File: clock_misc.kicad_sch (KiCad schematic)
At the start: 12 parts, among them Y1 Osc60MHz

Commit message: schematic wip
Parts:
- removed C56: 0.1uF, Capacitor_SMD:C_0402_1005Metric, symbol Device:C
- removed FID1, FID2, FID3, FID4: Fiducial, Fiducial:Fiducial_0.5mm_Mask1mm, symbol Mechanical:Fiducial
- removed Y1: Osc60MHz, Crystal:Crystal_SMD_3225-4Pin_3.2x2.5mm, symbol support_hardware:DSC60xx
- added C159 (x3), C39 (x2): 1uF, Capacitor_SMD:C_0402_1005Metric, symbol Device:C
- added R103, R104, R105, R106, R34, R35, R36: 330, Resistor_SMD:R_0402_1005Metric, symbol Device:R
- added U19 (x2): 74LVC1G06, Package_TO_SOT_SMD:SOT-353_SC-70-5, symbol 74xGxx:74LVC1G06
- added U20: 74LVC1G80, Package_TO_SOT_SMD:SOT-353_SC-70-5, symbol 74xGxx:74AUP1G80
- added U21: FANOUT, symbol support_hardware:74AVC9112
- added Y1: TCXO, Oscillator:Oscillator_SMD_Kyocera_KC2520Z-4Pin_2.5x2.0mm, symbol Oscillator:SG-210SCD
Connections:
- net +3V3: now also C39.1, C39.1, U21.1 (VCC), Y1.1 (OE), Y1.4 (Vcc)
- net GND: now also C159.2, C159.2, C159.2, C39.2, C39.2, U19.3 (GND), U19.3 (GND), U20.3 (GND), U21.3 (~{OE}), U21.4 (GND), Y1.2 (GND)
- net FPGA_CLK: now reaches R45.2
- net CLOCK_60MHZ: no longer names the net of TP34.1
- net CLOCK_60MHZ: now also U21.2 (A), Y1.3 (OUT); no longer R45.1
- new net: R105.1, U21.5 (Y1)
- new net: R104.1, U21.6 (Y2)
- new net: R103.1, U21.7 (Y3)
- new net: R45.1, U21.8 (Y4)
- new net: R36.2, U20.1 (D), U20.4 (~{Q})
- new net: R34.1, R35.1, U19.4
- new net: R106.1, U19.4
- new net 3V3RX: C159.1, C159.1, U19.5 (VCC), U20.5 (VCC)
- new net 3V3TX: C159.1, U19.5 (VCC)
- new net AFE_CLK: R103.2
- new net RX_CLK: R104.2, U19.2, U20.2 (C)
- new net RX_MIX_CLK: R106.2
- new net RX_RCVR_CLK: R36.1
- new net TX_CLK: R105.2, U19.2
- new net TX_MIX_CLK: R35.2
- new net TX_XCVR_CLK: R34.2
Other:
- moved on the sheet: H1, H2, H3, H4, R45, TP34

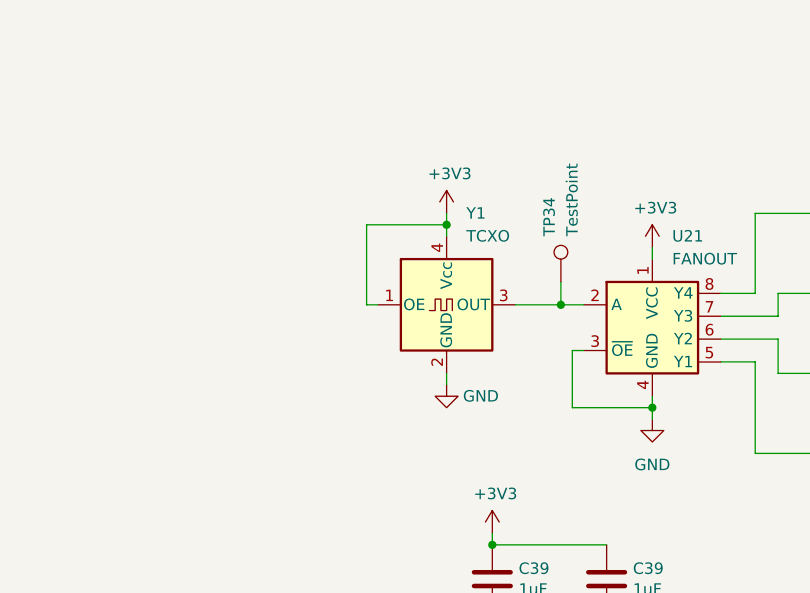
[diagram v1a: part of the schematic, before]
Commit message: add SWH two-way RF test connectors
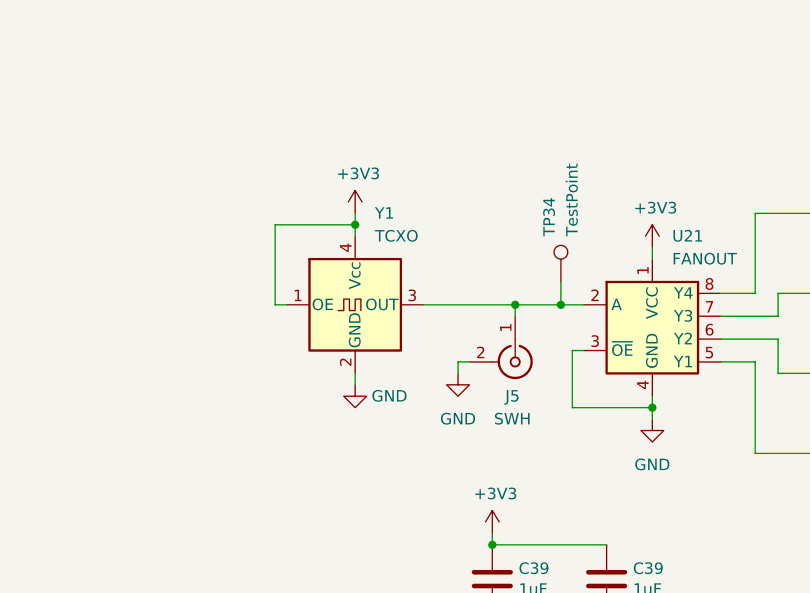
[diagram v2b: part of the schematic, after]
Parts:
- added J5: SWH, symbol Connector:Conn_Coaxial
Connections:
- net GND: now also J5.2 (Ext)
- net at TP34.1, U21.2 (A), Y1.3 (OUT): now also J5.1 (In)
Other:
- moved on the sheet: Y1
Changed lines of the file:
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@@
   (junction (at 241.3 77.47) (diameter 0) (color 0 0 0 0)
   )
-  (junction (at 71.12 67.31) (diameter 0) (color 0 0 0 0)
+  (junction (at 60.96 67.31) (diameter 0) (color 0 0 0 0)
   )
   (junction (at 173.99 123.19) (diameter 0) (color 0 0 0 0)
   )
+  (junction (at 78.74 76.2) (diameter 0) (color 0 0 0 0)
+  )
   (junction (at 40.64 168.91) (diameter 0) (color 0 0 0 0)
   )
@@
     (stroke (width 0) (type default))
   )
-  (wire (pts (xy 63.5 76.2) (xy 62.23 76.2))
+  (wire (pts (xy 53.34 76.2) (xy 52.07 76.2))
+    (stroke (width 0) (type default))
+  )
+  (wire (pts (xy 72.39 82.55) (xy 72.39 83.82))
     (stroke (width 0) (type default))
   )
@@
     (stroke (width 0) (type default))
   )
-  (wire (pts (xy 71.12 67.31) (xy 71.12 68.58))
+  (wire (pts (xy 78.74 76.2) (xy 83.82 76.2))
+    (stroke (width 0) (type default))
+  )
+  (wire (pts (xy 60.96 67.31) (xy 60.96 68.58))
     (stroke (width 0) (type default))
   )
@@
     (stroke (width 0) (type default))
   )
-  (wire (pts (xy 71.12 66.04) (xy 71.12 67.31))
+  (wire (pts (xy 60.96 66.04) (xy 60.96 67.31))
     (stroke (width 0) (type default))
   )
@@
     (stroke (width 0) (type default))
   )
-  (wire (pts (xy 62.23 76.2) (xy 62.23 67.31))
+  (wire (pts (xy 52.07 76.2) (xy 52.07 67.31))
     (stroke (width 0) (type default))
   )
@@
     (stroke (width 0) (type default))
   )
+  (wire (pts (xy 73.66 82.55) (xy 72.39 82.55))
+    (stroke (width 0) (type default))
+  )
   (wire (pts (xy 143.51 39.37) (xy 143.51 22.86))
     (stroke (width 0) (type default))
@@
     (stroke (width 0) (type default))
   )
-  (wire (pts (xy 78.74 76.2) (xy 83.82 76.2))
+  (wire (pts (xy 68.58 76.2) (xy 78.74 76.2))
     (stroke (width 0) (type default))
   )
@@
     (stroke (width 0) (type default))
   )
+  (wire (pts (xy 78.74 76.2) (xy 78.74 77.47))
+    (stroke (width 0) (type default))
+  )
   (wire (pts (xy 119.38 83.82) (xy 143.51 83.82))
     (stroke (width 0) (type default))
@@
     (stroke (width 0) (type default))
   )
-  (wire (pts (xy 62.23 67.31) (xy 71.12 67.31))
+  (wire (pts (xy 52.07 67.31) (xy 60.96 67.31))
     (stroke (width 0) (type default))
   )
@@
     (stroke (width 0) (type default))
   )
-  (wire (pts (xy 71.12 85.09) (xy 71.12 83.82))
+  (wire (pts (xy 60.96 85.09) (xy 60.96 83.82))
     (stroke (width 0) (type default))
   )
@@
     )
   )
-  (symbol (lib_id "power:+3V3") (at 71.12 66.04 0) (unit 1)
+  (symbol (lib_id "power:+3V3") (at 60.96 66.04 0) (unit 1)
     (in_bom yes) (on_board yes) (dnp no)
-    (property "Reference" "#PWR0170" (at 71.12 69.85 0)
-      (effects (font (size 1.27 1.27)) hide)
-    )
-    (property "Value" "+3V3" (at 71.4756 61.6458 0)
-      (effects (font (size 1.27 1.27)))
-    )
-    (property "Footprint" "" (at 71.12 66.04 0)
-      (effects (font (size 1.27 1.27)) hide)
-    )
-    (property "Datasheet" "" (at 71.12 66.04 0)
+    (property "Reference" "#PWR0170" (at 60.96 69.85 0)
+      (effects (font (size 1.27 1.27)) hide)
+    )
+    (property "Value" "+3V3" (at 61.3156 61.6458 0)
+      (effects (font (size 1.27 1.27)))
+    )
+    (property "Footprint" "" (at 60.96 66.04 0)
+      (effects (font (size 1.27 1.27)) hide)
+    )
+    (property "Datasheet" "" (at 60.96 66.04 0)
       (effects (font (size 1.27 1.27)) hide)
     )
@@
     )
   )
+  (symbol (lib_id "Connector:Conn_Coaxial") (at 78.74 82.55 270) (unit 1)
+    (in_bom yes) (on_board yes) (dnp no) (fields_autoplaced)
+    (property "Reference" "J5" (at 78.4468 86.36 90)
+      (effects (font (size 1.27 1.27)))
+    )
+    (property "Value" "SWH" (at 78.4468 88.9 90)
+      (effects (font (size 1.27 1.27)))
+    )
+    (property "Footprint" "" (at 78.74 82.55 0)
+      (effects (font (size 1.27 1.27)) hide)
+    )
+    (property "Datasheet" " ~" (at 78.74 82.55 0)
+      (effects (font (size 1.27 1.27)) hide)
+    )
+    (property "Description" "COAX CONN TWO-WAY" (at 78.74 82.55 0)
+      (effects (font (size 1.27 1.27)) hide)
+    )
+    (property "Manufacturer" "Murata" (at 78.74 82.55 0)
+      (effects (font (size 1.27 1.27)) hide)
+    )
+    (property "Part Number" "MM8930-2620RJ4" (at 78.74 82.55 0)
+      (effects (font (size 1.27 1.27)) hide)
+    )
+    (property "Substitution" "MM8930-2620RK15" (at 78.74 82.55 0)
+      (effects (font (size 1.27 1.27)) hide)
+    )
+    (pin "1")
+    (pin "2")
+    (instances
+      (project "mainboard"
+        (path "/fb621148-8145-4217-9712-738e1b5a4823/4ec621be-184d-4855-a96d-f6fa2a788a77/90da2209-0e18-4bd4-8ef6-3d6f9ed46ff8"
+          (reference "J5") (unit 1)
+        )
+        (path "/fb621148-8145-4217-9712-738e1b5a4823/4ec621be-184d-4855-a96d-f6fa2a788a77/6aa278c8-8281-4438-81b7-90e6d7ac4f12"
+          (reference "J11") (unit 1)
+        )
+        (path "/fb621148-8145-4217-9712-738e1b5a4823/07741d92-cb3b-401f-9c7e-29f688af7269"
+          (reference "J12") (unit 1)
+        )
+      )
+    )
+  )
   (symbol (lib_id "support_hardware:3V3TX") (at 154.94 111.76 0) (unit 1)
     (in_bom yes) (on_board yes) (dnp no) (fields_autoplaced)
@@
     )
   )
-  (symbol (lib_id "power:GND") (at 71.12 85.09 0) (unit 1)
+  (symbol (lib_id "power:GND") (at 60.96 85.09 0) (unit 1)
     (in_bom yes) (on_board yes) (dnp no)
-    (property "Reference" "#PWR0173" (at 71.12 91.44 0)
-      (effects (font (size 1.27 1.27)) hide)
-    )
-    (property "Value" "GND" (at 74.93 86.36 0)
-      (effects (font (size 1.27 1.27)))
-    )
-    (property "Footprint" "" (at 71.12 85.09 0)
-      (effects (font (size 1.27 1.27)) hide)
-    )
-    (property "Datasheet" "" (at 71.12 85.09 0)
+    (property "Reference" "#PWR0173" (at 60.96 91.44 0)
+      (effects (font (size 1.27 1.27)) hide)
+    )
+    (property "Value" "GND" (at 64.77 86.36 0)
+      (effects (font (size 1.27 1.27)))
+    )
+    (property "Footprint" "" (at 60.96 85.09 0)
+      (effects (font (size 1.27 1.27)) hide)
+    )
+    (property "Datasheet" "" (at 60.96 85.09 0)
       (effects (font (size 1.27 1.27)) hide)
     )
@@
     )
   )
-  (symbol (lib_id "Oscillator:SG-210SCD") (at 71.12 76.2 0) (unit 1)
-    (in_bom yes) (on_board yes) (dnp no) (fields_autoplaced)
-    (property "Reference" "Y1" (at 73.3141 66.04 0)
-      (effects (font (size 1.27 1.27)) (justify left))
-    )
-    (property "Value" "TCXO" (at 73.3141 68.58 0)
-      (effects (font (size 1.27 1.27)) (justify left))
-    )
-    (property "Footprint" "Oscillator:Oscillator_SMD_Kyocera_KC2520Z-4Pin_2.5x2.0mm" (at 71.12 95.25 0)
-      (effects (font (size 1.27 1.27)) hide)
-    )
-    (property "Datasheet" "https://www.raltron.com/webproducts/specs/TCXO/RTXE-2520ED333-C-40.000-TR.pdf" (at 71.12 76.2 0)
-      (effects (font (size 1.27 1.27)) hide)
-    )
-    (property "Description" "XTAL OSC TCXO 40MHZ 3.3V HCMOS" (at 71.12 76.2 0)
-      (effects (font (size 1.27 1.27)) hide)
-    )
-    (property "Manufacturer" "Raltron" (at 71.12 76.2 0)
-      (effects (font (size 1.27 1.27)) hide)
-    )
-    (property "Part Number" "RTXE-2520ED333-C-40.000-TR" (at 71.12 76.2 0)
-      (effects (font (size 1.27 1.27)) hide)
-    )
+  (symbol (lib_id "power:GND") (at 72.39 83.82 0) (unit 1)
+    (in_bom yes) (on_board yes) (dnp no) (fields_autoplaced)
+    (property "Reference" "#PWR023" (at 72.39 90.17 0)
+      (effects (font (size 1.27 1.27)) hide)
+    )
+    (property "Value" "GND" (at 72.39 88.9 0)
+      (effects (font (size 1.27 1.27)))
+    )
+    (property "Footprint" "" (at 72.39 83.82 0)
+      (effects (font (size 1.27 1.27)) hide)
+    )
+    (property "Datasheet" "" (at 72.39 83.82 0)
+      (effects (font (size 1.27 1.27)) hide)
+    )
+    (pin "1")
+    (instances
+      (project "ununs"
+        (path "/a05d7640-f2f6-4ba7-8c51-5a4af431fc13"
+          (reference "#PWR023") (unit 1)
+        )
+      )
+      (project "mainboard"
+        (path "/fb621148-8145-4217-9712-738e1b5a4823/4ec621be-184d-4855-a96d-f6fa2a788a77/90da2209-0e18-4bd4-8ef6-3d6f9ed46ff8"
+          (reference "#PWR0158") (unit 1)
+        )
+        (path "/fb621148-8145-4217-9712-738e1b5a4823/4ec621be-184d-4855-a96d-f6fa2a788a77/6aa278c8-8281-4438-81b7-90e6d7ac4f12"
+          (reference "#PWR0303") (unit 1)
+        )
+        (path "/fb621148-8145-4217-9712-738e1b5a4823/07741d92-cb3b-401f-9c7e-29f688af7269"
+          (reference "#PWR0304") (unit 1)
+        )
+      )
+    )
+  )
+  (symbol (lib_id "Oscillator:SG-210SCD") (at 60.96 76.2 0) (unit 1)
+    (in_bom yes) (on_board yes) (dnp no) (fields_autoplaced)
+    (property "Reference" "Y1" (at 63.1541 66.04 0)
+      (effects (font (size 1.27 1.27)) (justify left))
+    )
+    (property "Value" "TCXO" (at 63.1541 68.58 0)
+      (effects (font (size 1.27 1.27)) (justify left))
+    )
+    (property "Footprint" "Oscillator:Oscillator_SMD_Kyocera_KC2520Z-4Pin_2.5x2.0mm" (at 60.96 95.25 0)
+      (effects (font (size 1.27 1.27)) hide)
+    )
+    (property "Datasheet" "https://www.raltron.com/webproducts/specs/TCXO/RTXE-2520ED333-C-40.000-TR.pdf" (at 60.96 76.2 0)
+      (effects (font (size 1.27 1.27)) hide)
+    )
+    (property "Description" "XTAL OSC TCXO 40MHZ 3.3V HCMOS" (at 60.96 76.2 0)
+      (effects (font (size 1.27 1.27)) hide)
+    )
+    (property "Manufacturer" "Raltron" (at 60.96 76.2 0)
+      (effects (font (size 1.27 1.27)) hide)
+    )
+    (property "Part Number" "RTXE-2520ED333-C-40.000-TR" (at 60.96 76.2 0)
+      (effects (font (size 1.27 1.27)) hide)
+    )

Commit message: update symbol metadata
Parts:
- U21: Manufacturer (none) -> Nexperia; Part Number (none) -> 74AVC9112GTX
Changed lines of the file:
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@@
       (effects (font (size 1.27 1.27)) hide)
     )
-    (property "Datasheet" "" (at 93.98 78.74 0)
+    (property "Datasheet" "https://assets.nexperia.com/documents/data-sheet/74AVC9112.pdf" (at 93.98 78.74 0)
       (effects (font (size 1.27 1.27)) hide)
     )
+    (property "Manufacturer" "Nexperia" (at 93.98 78.74 0)
+      (effects (font (size 1.27 1.27)) hide)
+    )
+    (property "Description" "IC CLK BUFFER 1:4 8XSON" (at 93.98 78.74 0)
+      (effects (font (size 1.27 1.27)) hide)
+    )
+    (property "Part Number" "74AVC9112GTX" (at 93.98 78.74 0)
+      (effects (font (size 1.27 1.27)) hide)
+    )

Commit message: add SWH connector symbols
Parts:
- removed J5: SWH, symbol Connector:Conn_Coaxial
- added J5: SWH, symbol radio:Conn_Coaxial_MM8930-2620
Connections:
- net GND: now also J5.3 (Ext)
- net at TP34.1, U21.2 (A): now also J5.2 (R); no longer Y1.3 (OUT)
- new net: J5.1 (C), Y1.3 (OUT)
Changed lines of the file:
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@@
   (junction (at 173.99 123.19) (diameter 0) (color 0 0 0 0)
   )
-  (junction (at 78.74 76.2) (diameter 0) (color 0 0 0 0)
-  )
   (junction (at 40.64 168.91) (diameter 0) (color 0 0 0 0)
   )
@@
     (stroke (width 0) (type default))
   )
-  (wire (pts (xy 72.39 82.55) (xy 72.39 83.82))
+  (wire (pts (xy 76.2 81.28) (xy 76.2 82.55))
     (stroke (width 0) (type default))
   )
@@
     (stroke (width 0) (type default))
   )
-  (wire (pts (xy 78.74 76.2) (xy 83.82 76.2))
-    (stroke (width 0) (type default))
-  )
   (wire (pts (xy 60.96 67.31) (xy 60.96 68.58))
     (stroke (width 0) (type default))
@@
     (stroke (width 0) (type default))
   )
+  (wire (pts (xy 68.58 76.2) (xy 71.12 76.2))
+    (stroke (width 0) (type default))
+  )
   (wire (pts (xy 105.41 66.04) (xy 111.76 66.04))
     (stroke (width 0) (type default))
@@
     (stroke (width 0) (type default))
   )
+  (wire (pts (xy 81.28 76.2) (xy 83.82 76.2))
+    (stroke (width 0) (type default))
+  )
   (wire (pts (xy 119.38 74.93) (xy 120.65 74.93))
     (stroke (width 0) (type default))
@@
     (stroke (width 0) (type default))
   )
-  (wire (pts (xy 73.66 82.55) (xy 72.39 82.55))
-    (stroke (width 0) (type default))
-  )
   (wire (pts (xy 143.51 39.37) (xy 143.51 22.86))
     (stroke (width 0) (type default))
@@
     (stroke (width 0) (type default))
   )
-  (wire (pts (xy 68.58 76.2) (xy 78.74 76.2))
-    (stroke (width 0) (type default))
-  )
   (wire (pts (xy 171.45 39.37) (xy 170.18 39.37))
     (stroke (width 0) (type default))
@@
   )
   (wire (pts (xy 172.72 123.19) (xy 173.99 123.19))
-    (stroke (width 0) (type default))
-  )
-  (wire (pts (xy 78.74 76.2) (xy 78.74 77.47))
     (stroke (width 0) (type default))
   )
@@
     )
   )
-  (symbol (lib_id "Connector:Conn_Coaxial") (at 78.74 82.55 270) (unit 1)
-    (in_bom yes) (on_board yes) (dnp no) (fields_autoplaced)
-    (property "Reference" "J5" (at 78.4468 86.36 90)
-      (effects (font (size 1.27 1.27)))
-    )
-    (property "Value" "SWH" (at 78.4468 88.9 90)
-      (effects (font (size 1.27 1.27)))
-    )
-    (property "Footprint" "" (at 78.74 82.55 0)
-      (effects (font (size 1.27 1.27)) hide)
-    )
-    (property "Datasheet" " ~" (at 78.74 82.55 0)
-      (effects (font (size 1.27 1.27)) hide)
-    )
-    (property "Description" "COAX CONN TWO-WAY" (at 78.74 82.55 0)
-      (effects (font (size 1.27 1.27)) hide)
-    )
-    (property "Manufacturer" "Murata" (at 78.74 82.55 0)
-      (effects (font (size 1.27 1.27)) hide)
-    )
-    (property "Part Number" "MM8930-2620RJ4" (at 78.74 82.55 0)
-      (effects (font (size 1.27 1.27)) hide)
-    )
-    (property "Substitution" "MM8930-2620RK15" (at 78.74 82.55 0)
-      (effects (font (size 1.27 1.27)) hide)
-    )
-    (pin "1")
-    (pin "2")
-    (instances
-      (project "mainboard"
-        (path "/fb621148-8145-4217-9712-738e1b5a4823/4ec621be-184d-4855-a96d-f6fa2a788a77/90da2209-0e18-4bd4-8ef6-3d6f9ed46ff8"
-          (reference "J5") (unit 1)
-        )
-        (path "/fb621148-8145-4217-9712-738e1b5a4823/4ec621be-184d-4855-a96d-f6fa2a788a77/6aa278c8-8281-4438-81b7-90e6d7ac4f12"
-          (reference "J11") (unit 1)
-        )
-        (path "/fb621148-8145-4217-9712-738e1b5a4823/07741d92-cb3b-401f-9c7e-29f688af7269"
-          (reference "J12") (unit 1)
-        )
-      )
-    )
-  )
   (symbol (lib_id "support_hardware:3V3TX") (at 154.94 111.76 0) (unit 1)
     (in_bom yes) (on_board yes) (dnp no) (fields_autoplaced)
@@
     )
   )
+  (symbol (lib_id "radio:Conn_Coaxial_MM8930-2620") (at 76.2 76.2 0) (unit 1)
+    (in_bom yes) (on_board yes) (dnp no) (fields_autoplaced)
+    (property "Reference" "J5" (at 76.2 68.58 0)
+      (effects (font (size 1.27 1.27)))
+    )
+    (property "Value" "SWH" (at 76.2 71.12 0)
+      (effects (font (size 1.27 1.27)))
+    )
+    (property "Footprint" "" (at 76.2 76.2 0)
+      (effects (font (size 1.27 1.27)) hide)
+    )
+    (property "Datasheet" "https://www.murata.com/-/media/webrenewal/support/library/catalog/products/connector/o30e.ashx" (at 76.2 76.2 0)
+      (effects (font (size 1.27 1.27)) hide)
+    )
+    (property "Description" "COAX CONN TWO-WAY" (at 76.2 76.2 0)
+      (effects (font (size 1.27 1.27)) hide)
+    )
+    (property "Manufacturer" "Murata" (at 76.2 76.2 0)
+      (effects (font (size 1.27 1.27)) hide)
+    )
+    (property "Part Number" "MM8930-2620RJ4" (at 76.2 76.2 0)
+      (effects (font (size 1.27 1.27)) hide)
+    )
+    (property "Substitution" "MM8930-2620RK15" (at 76.2 76.2 0)
+      (effects (font (size 1.27 1.27)) hide)
+    )
+    (pin "2")
+    (pin "1")
+    (pin "3")
+    (instances
+      (project "mainboard"
+        (path "/fb621148-8145-4217-9712-738e1b5a4823/4ec621be-184d-4855-a96d-f6fa2a788a77/90da2209-0e18-4bd4-8ef6-3d6f9ed46ff8"
+          (reference "J5") (unit 1)
+        )
+        (path "/fb621148-8145-4217-9712-738e1b5a4823/07741d92-cb3b-401f-9c7e-29f688af7269"
+          (reference "J12") (unit 1)
+        )
+      )
+    )
+  )
   (symbol (lib_id "power:GND") (at 76.2 111.76 0) (unit 1)
     (in_bom yes) (on_board yes) (dnp no)
@@
     )
   )
-  (symbol (lib_id "power:GND") (at 72.39 83.82 0) (unit 1)
-    (in_bom yes) (on_board yes) (dnp no) (fields_autoplaced)
-    (property "Reference" "#PWR023" (at 72.39 90.17 0)
-      (effects (font (size 1.27 1.27)) hide)
-    )
-    (property "Value" "GND" (at 72.39 88.9 0)
-      (effects (font (size 1.27 1.27)))
-    )
-    (property "Footprint" "" (at 72.39 83.82 0)
-      (effects (font (size 1.27 1.27)) hide)
-    )
-    (property "Datasheet" "" (at 72.39 83.82 0)
-      (effects (font (size 1.27 1.27)) hide)
-    )
+  (symbol (lib_id "power:GND") (at 76.2 82.55 0) (unit 1)
+    (in_bom yes) (on_board yes) (dnp no) (fields_autoplaced)
+    (property "Reference" "#PWR023" (at 76.2 88.9 0)
+      (effects (font (size 1.27 1.27)) hide)
+    )
+    (property "Value" "GND" (at 76.2 87.63 0)
+      (effects (font (size 1.27 1.27)))
+    )
+    (property "Footprint" "" (at 76.2 82.55 0)
+      (effects (font (size 1.27 1.27)) hide)
+    )
+    (property "Datasheet" "" (at 76.2 82.55 0)
+      (effects (font (size 1.27 1.27)) hide)
+    )
